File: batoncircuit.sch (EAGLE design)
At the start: 19 parts, among them IC1 74LS595D, IC2 4543D, IC3 4543D, IC5 RFD22301, IC6 TLC555CD, IC8-LP3872 786TV, U8 V321-3DIGIT-LCD

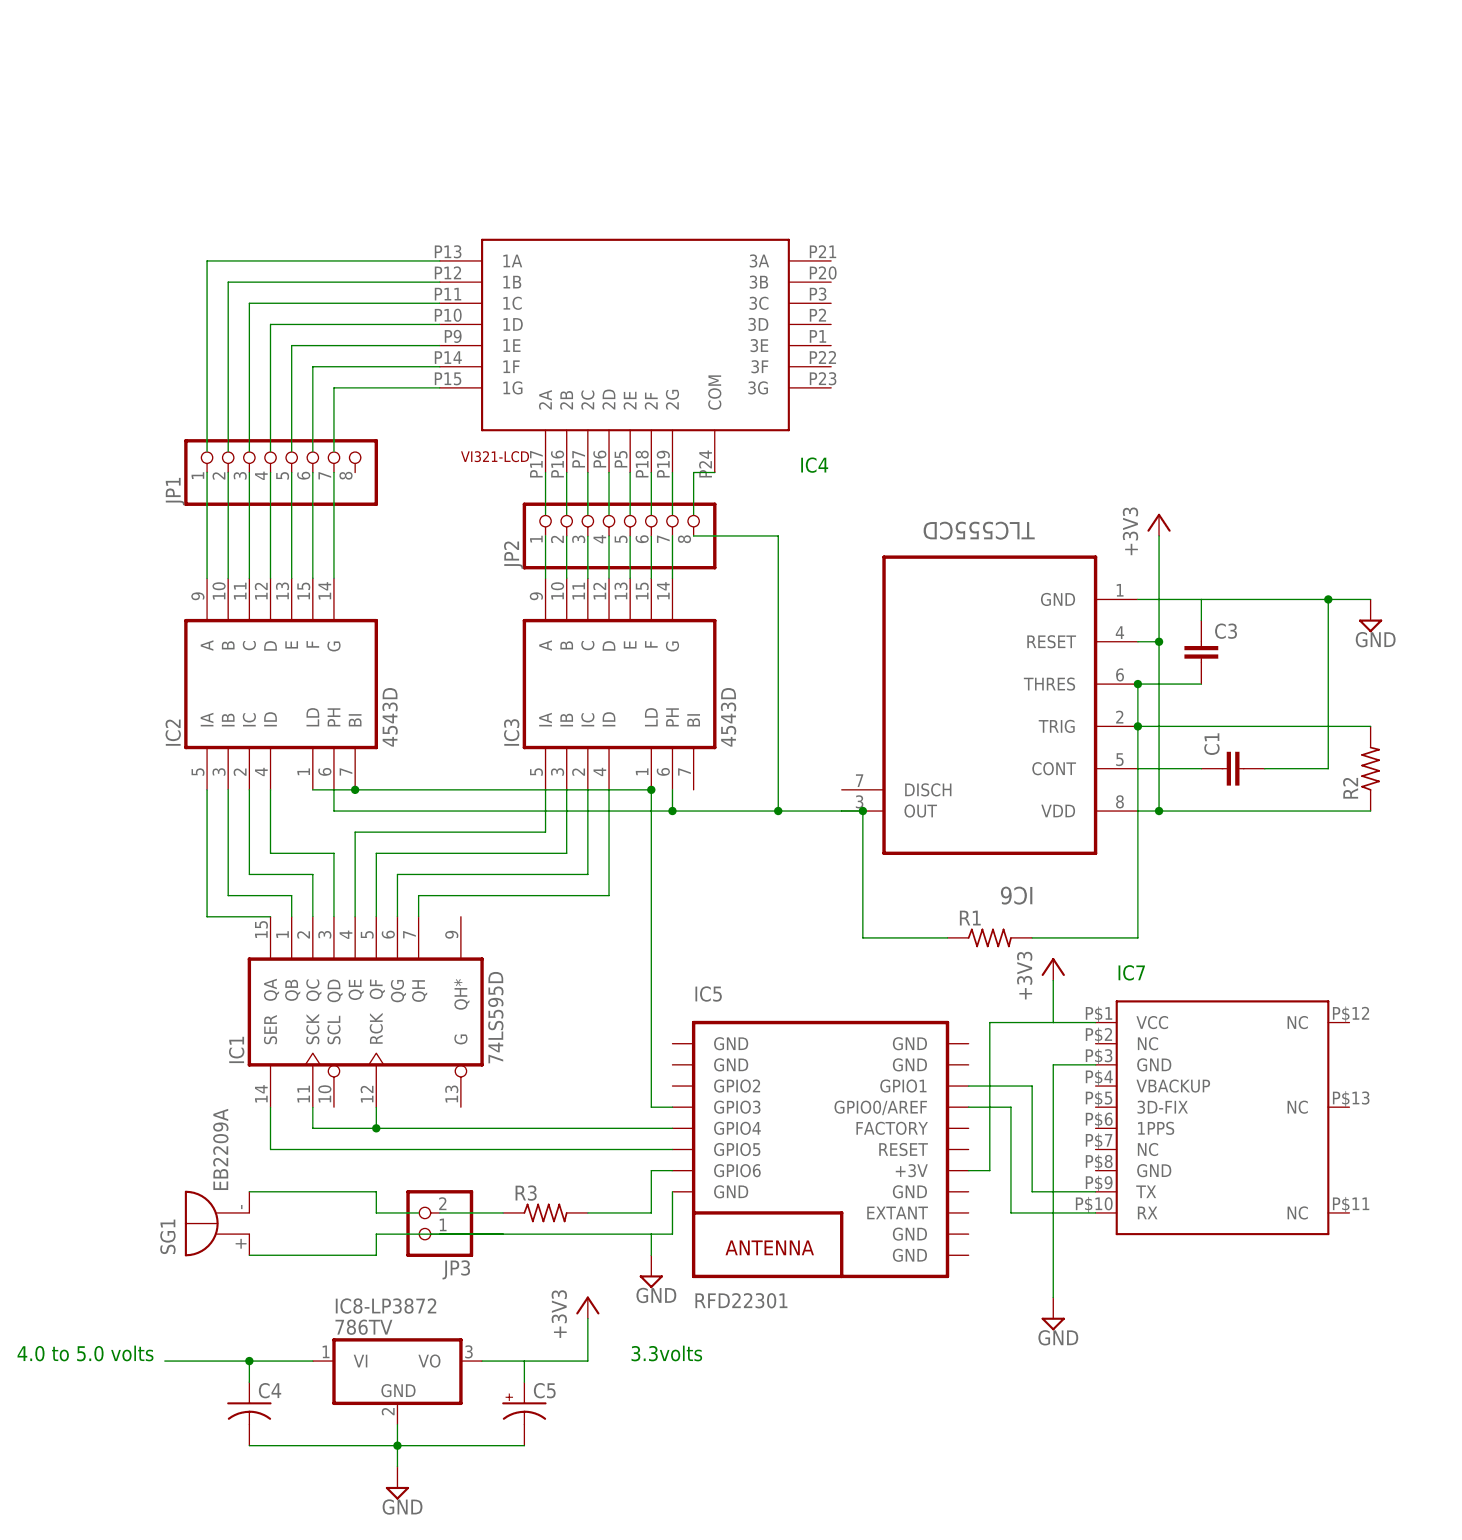
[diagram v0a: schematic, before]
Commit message: Switches and jack addition
Added power jack, marker switch and power switch along with connecting
pins on board.
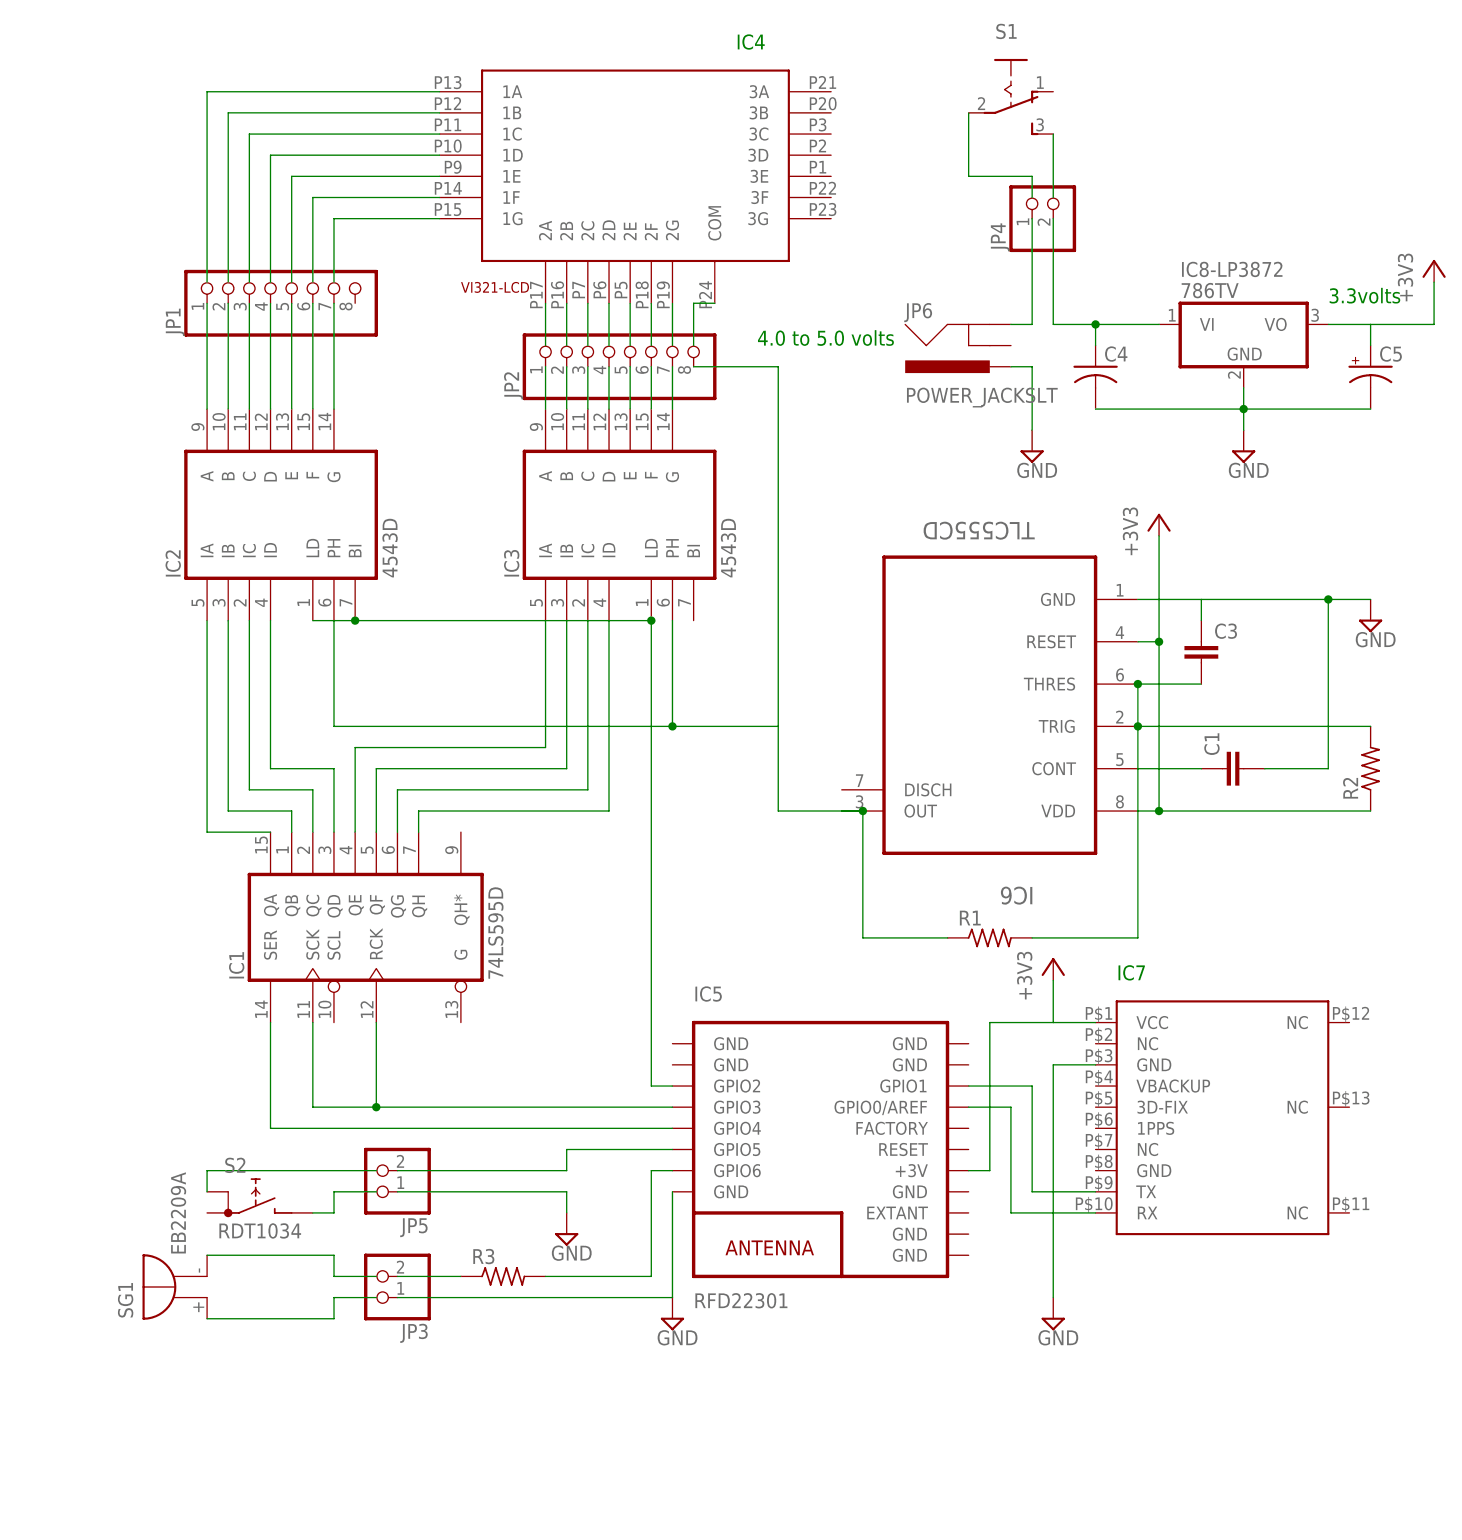
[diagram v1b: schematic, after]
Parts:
- added JP4, JP5: (no value), pinhead:PINHD-1X2
- added JP6: POWER_JACKSLT, SparkFun-Connectors:POWER_JACKSLT
- added S1: (no value), switch:255SB
- added S2: RDT1034, switch:RDT1034
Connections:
- new net N$51: C5.+, IC8-LP3872.VO
- new net N$52: JP4.1, JP6.GND
- new net N$53: S1.S
- new net N$54: S1.P
- new net N$55: IC5.GPIO5, JP5.2
- new net N$56: S2.B
- new net N$57: S2.A
- net +3V3: no longer C5.+, IC8-LP3872.VO
- net GND: now also JP5.1, JP6.PWR
- net N$24: now also IC5.GPIO4; no longer IC5.GPIO5
- net N$29: now also IC5.GPIO2; no longer IC5.GPIO3
- net N$31: now also JP4.2
- net N$34: now also IC5.GPIO3; no longer IC5.GPIO4
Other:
- moved on the sheet: C4, C5, IC1, IC2, IC3, IC8-LP3872, JP1, JP2, JP3, R3, SG1
